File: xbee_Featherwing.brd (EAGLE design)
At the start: 76.2 x 30.5 mm, 17 parts

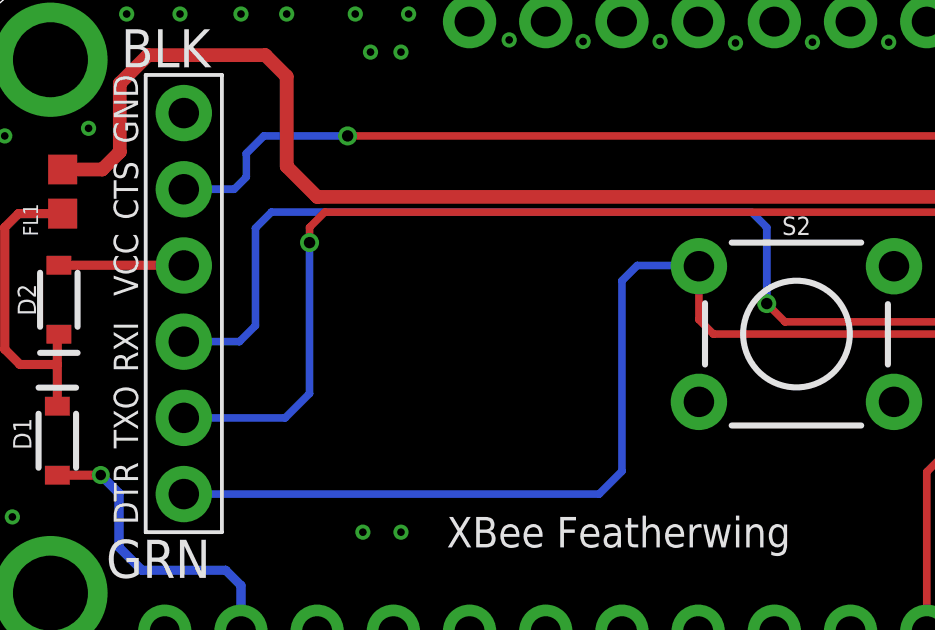
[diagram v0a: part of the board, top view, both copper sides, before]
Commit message: Changing footprint
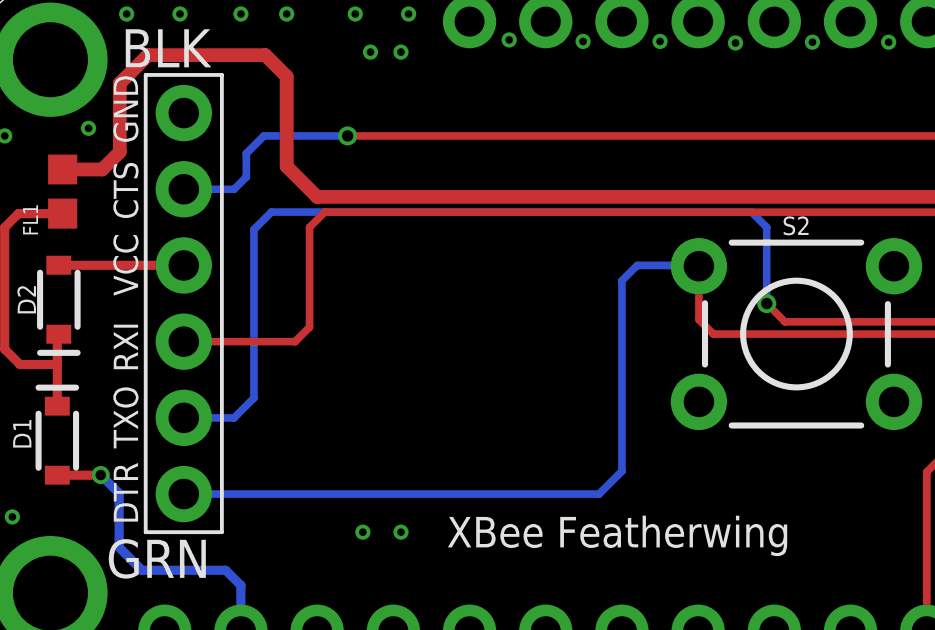
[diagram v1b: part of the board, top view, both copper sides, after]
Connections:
- net DIN: now also J1.P$3; no longer J1.P$2
- net DOUT: now also J1.P$2; no longer J1.P$3
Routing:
- net DOUT: track 124.1 -> 126.5 mm
- net DIN: track 150.3 -> 148.0 mm, vias 4 -> 3
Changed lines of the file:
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@@
 <?xml version="1.0" encoding="utf-8"?>
 <!DOCTYPE eagle SYSTEM "eagle.dtd">
-<eagle version="9.5.0">
+<eagle version="9.4.1">
 <drawing>
 <settings>
@@
 <signal name="DOUT">
 <contactref element="JP1" pad="2"/>
-<contactref element="J1" pad="P$3"/>
 <contactref element="MS1" pad="14"/>
 <wire x1="39.37" y1="1.27" x2="39.37" y2="3.81" width="0.254" layer="1"/>
@@
 <wire x1="26.416" y1="12.192" x2="26.416" y2="14.732" width="0.254" layer="16"/>
 <wire x1="26.416" y1="14.732" x2="25.908" y2="15.24" width="0.254" layer="16"/>
-<wire x1="25.908" y1="15.24" x2="14.986" y2="15.24" width="0.254" layer="16"/>
-<wire x1="14.986" y1="15.24" x2="14.732" y2="15.24" width="0.254" layer="16"/>
+<wire x1="25.908" y1="15.24" x2="9.906" y2="15.24" width="0.254" layer="16"/>
 <wire x1="70.104" y1="15.5448" x2="69.5452" y2="14.986" width="0.254" layer="1"/>
 <wire x1="46.99" y1="14.478" x2="46.99" y2="12.0904" width="0.254" layer="1"/>
-<wire x1="14.732" y1="15.24" x2="9.906" y2="15.24" width="0.254" layer="16"/>
-<wire x1="8.8392" y1="10.922" x2="6.985" y2="10.922" width="0.254" layer="16"/>
-<wire x1="9.906" y1="15.24" x2="9.3726" y2="14.7066" width="0.254" layer="16"/>
-<wire x1="9.3726" y1="14.7066" x2="9.3726" y2="11.4554" width="0.254" layer="16"/>
-<wire x1="9.3726" y1="11.4554" x2="8.8392" y2="10.922" width="0.254" layer="16"/>
+<contactref element="J1" pad="P$2"/>
+<wire x1="9.906" y1="15.24" x2="9.3218" y2="14.6558" width="0.254" layer="16"/>
+<wire x1="8.6614" y1="8.382" x2="6.985" y2="8.382" width="0.254" layer="16"/>
+<wire x1="9.3218" y1="14.6558" x2="9.3218" y2="9.0424" width="0.254" layer="16"/>
+<wire x1="9.3218" y1="9.0424" x2="8.6614" y2="8.382" width="0.254" layer="16"/>
 </signal>
 <signal name="DIN">
 <contactref element="JP1" pad="3"/>
-<contactref element="J1" pad="P$2"/>
 <contactref element="MS1" pad="15"/>
 <wire x1="41.91" y1="1.27" x2="41.91" y2="2.032" width="0.254" layer="16"/>
@@
 <wire x1="43.688" y1="15.24" x2="11.684" y2="15.24" width="0.254" layer="1"/>
 <wire x1="11.684" y1="15.24" x2="11.176" y2="14.732" width="0.254" layer="1"/>
-<wire x1="11.176" y1="14.732" x2="11.176" y2="14.224" width="0.254" layer="1"/>
-<via x="11.176" y="14.224" extent="1-16" drill="0.381"/>
-<wire x1="11.176" y1="14.224" x2="11.176" y2="9.1948" width="0.254" layer="16"/>
-<wire x1="11.176" y1="9.1948" x2="10.3632" y2="8.382" width="0.254" layer="16"/>
-<wire x1="10.3632" y1="8.382" x2="6.985" y2="8.382" width="0.254" layer="16"/>
+<contactref element="J1" pad="P$3"/>
+<wire x1="11.176" y1="11.4046" x2="10.6934" y2="10.922" width="0.254" layer="1"/>
+<wire x1="10.6934" y1="10.922" x2="6.985" y2="10.922" width="0.254" layer="1"/>
+<wire x1="11.176" y1="14.732" x2="11.176" y2="11.4046" width="0.254" layer="1"/>
 </signal>
 <signal name="!RESET">
